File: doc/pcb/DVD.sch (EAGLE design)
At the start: 48 parts, among them IC1 7805, IC2 74HC14N

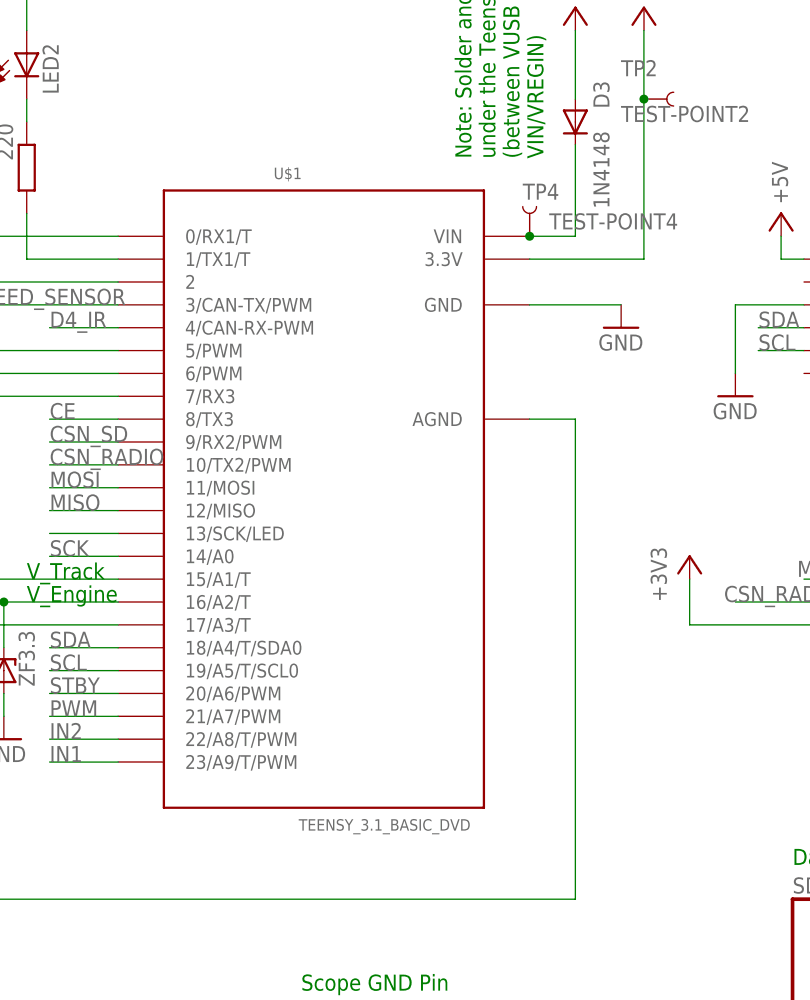
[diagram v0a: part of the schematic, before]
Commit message: bigger pads for Teensy
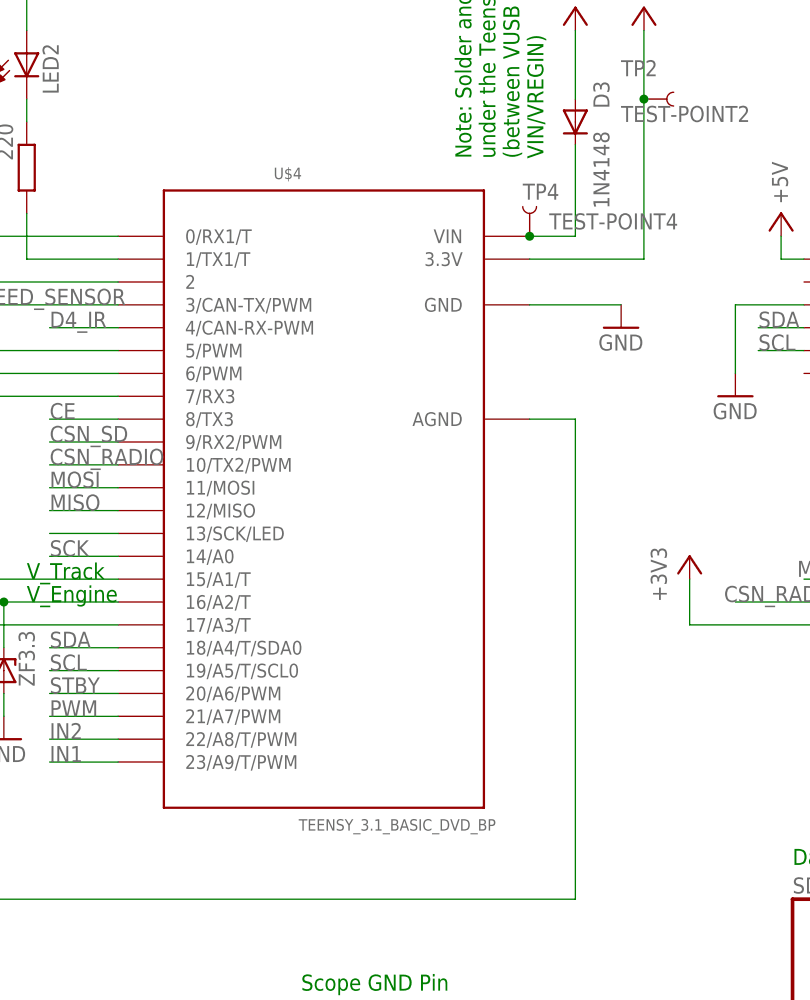
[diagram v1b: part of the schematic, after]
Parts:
- removed U$1: TEENSY_3.1_BASIC_DVD, Teensy_3_Series_Board_v1.0:TEENSY_3.1_BASIC_DVD
- added U$4: TEENSY_3.1_BASIC_DVD_BP, Teensy_3_Series_Board_v1.0:TEENSY_3.1_BASIC_DVD_BP
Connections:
- net +3V3: now also U$4.3.3V; no longer U$1.3.3V
- net AGND: now also U$4.AGND; no longer U$1.AGND
- net CE: now also U$4.8/TX3; no longer U$1.8/TX3
- net CSN_RADIO: now also U$4.10/TX2/PWM; no longer U$1.10/TX2/PWM
- net CSN_SD: now also U$4.9/RX2/PWM; no longer U$1.9/RX2/PWM
- net D4_IR: now also U$4.4/CAN-RX-PWM; no longer U$1.4/CAN-RX-PWM
- net GND: now also U$4.GND; no longer U$1.GND
- net IN1: now also U$4.23/A9/T/PWM; no longer U$1.23/A9/T/PWM
- net IN2: now also U$4.22/A8/T/PWM; no longer U$1.22/A8/T/PWM
- net MISO: now also U$4.12/MISO; no longer U$1.12/MISO
- net MOSI: now also U$4.11/MOSI; no longer U$1.11/MOSI
- net N$1: now also U$4.VIN; no longer U$1.VIN
- net N$10: now also U$4.15/A1/T; no longer U$1.15/A1/T
- net N$11: now also U$4.16/A2/T; no longer U$1.16/A2/T
- net N$18: now also U$4.0/RX1/T; no longer U$1.0/RX1/T
- net N$19: now also U$4.1/TX1/T; no longer U$1.1/TX1/T
- net N$20: now also U$4.2; no longer U$1.2
- net N$21: now also U$4.6/PWM; no longer U$1.6/PWM
- net N$22: now also U$4.7/RX3; no longer U$1.7/RX3
- net N$3: now also U$4.5/PWM; no longer U$1.5/PWM
- net N$6: now also U$4.17/A3/T; no longer U$1.17/A3/T
- net N$9: now also U$4.13/SCK/LED; no longer U$1.13/SCK/LED
- net PWM: now also U$4.21/A7/PWM; no longer U$1.21/A7/PWM
- net SCK: now also U$4.14/A0; no longer U$1.14/A0
- net SCL: now also U$4.19/A5/T/SCL0; no longer U$1.19/A5/T/SCL0
- net SDA: now also U$4.18/A4/T/SDA0; no longer U$1.18/A4/T/SDA0
- net SPEED_SENSOR: now also U$4.3/CAN-TX/PWM; no longer U$1.3/CAN-TX/PWM
- net STBY: now also U$4.20/A6/PWM; no longer U$1.20/A6/PWM

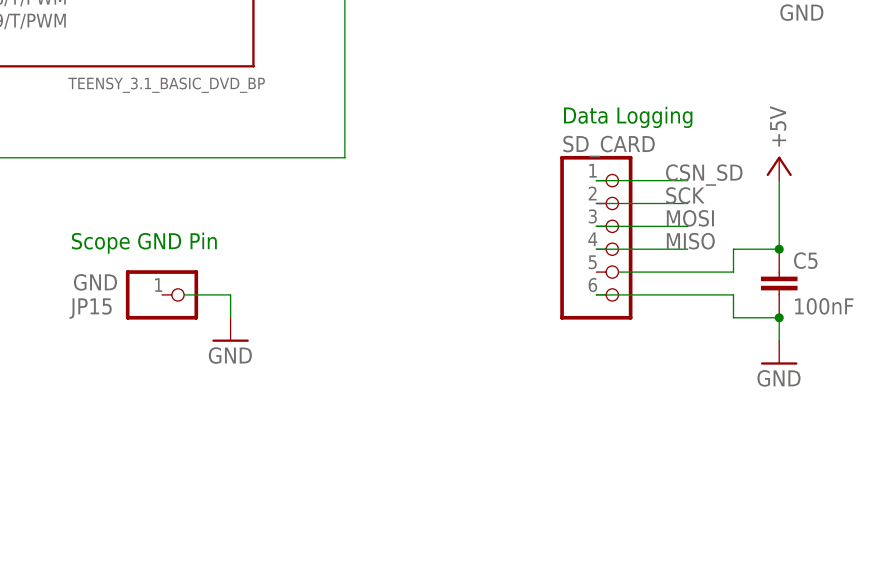
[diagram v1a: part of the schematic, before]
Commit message: Redrawn Chassis Picture, fixed schematic and created Board
Please review and give comments
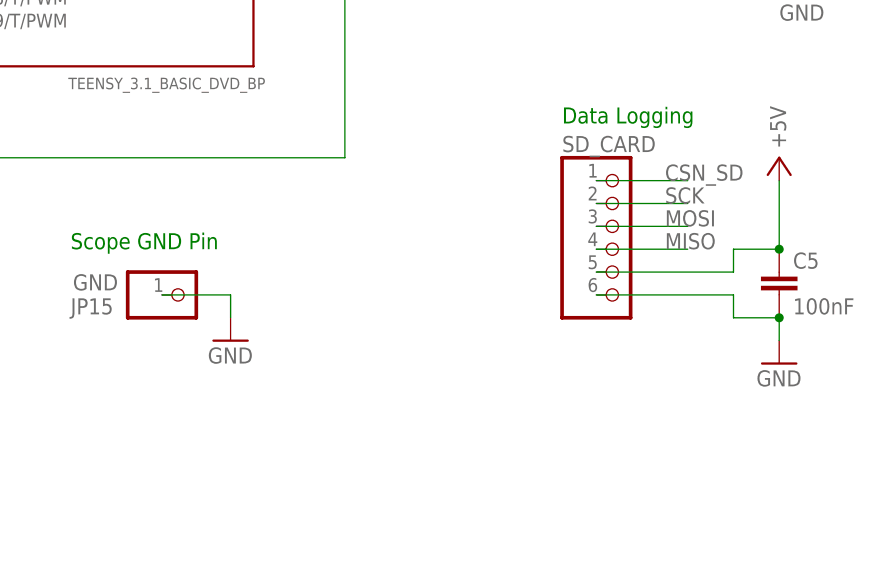
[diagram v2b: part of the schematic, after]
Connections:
- net +5V: now also SD_CARD.5
- net GND: now also JP15.1
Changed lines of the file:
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@@
 <segment>
 <pinref part="GND9" gate="1" pin="GND"/>
-<wire x1="139.7" y1="38.1" x2="144.78" y2="38.1" width="0.1524" layer="91"/>
+<wire x1="137.16" y1="38.1" x2="144.78" y2="38.1" width="0.1524" layer="91"/>
 <wire x1="144.78" y1="38.1" x2="144.78" y2="35.56" width="0.1524" layer="91"/>
+<pinref part="JP15" gate="G$1" pin="1"/>
 </segment>
 </net>
@@
 <pinref part="C5" gate="G$1" pin="1"/>
 <wire x1="205.74" y1="50.8" x2="205.74" y2="43.18" width="0.1524" layer="91"/>
-<wire x1="187.96" y1="40.64" x2="200.66" y2="40.64" width="0.1524" layer="91"/>
+<wire x1="185.42" y1="40.64" x2="200.66" y2="40.64" width="0.1524" layer="91"/>
 <wire x1="200.66" y1="40.64" x2="200.66" y2="43.18" width="0.1524" layer="91"/>
 <wire x1="200.66" y1="43.18" x2="205.74" y2="43.18" width="0.1524" layer="91"/>
 <junction x="205.74" y="43.18"/>
+<pinref part="SD_CARD" gate="A" pin="5"/>
 </segment>
 <segment>

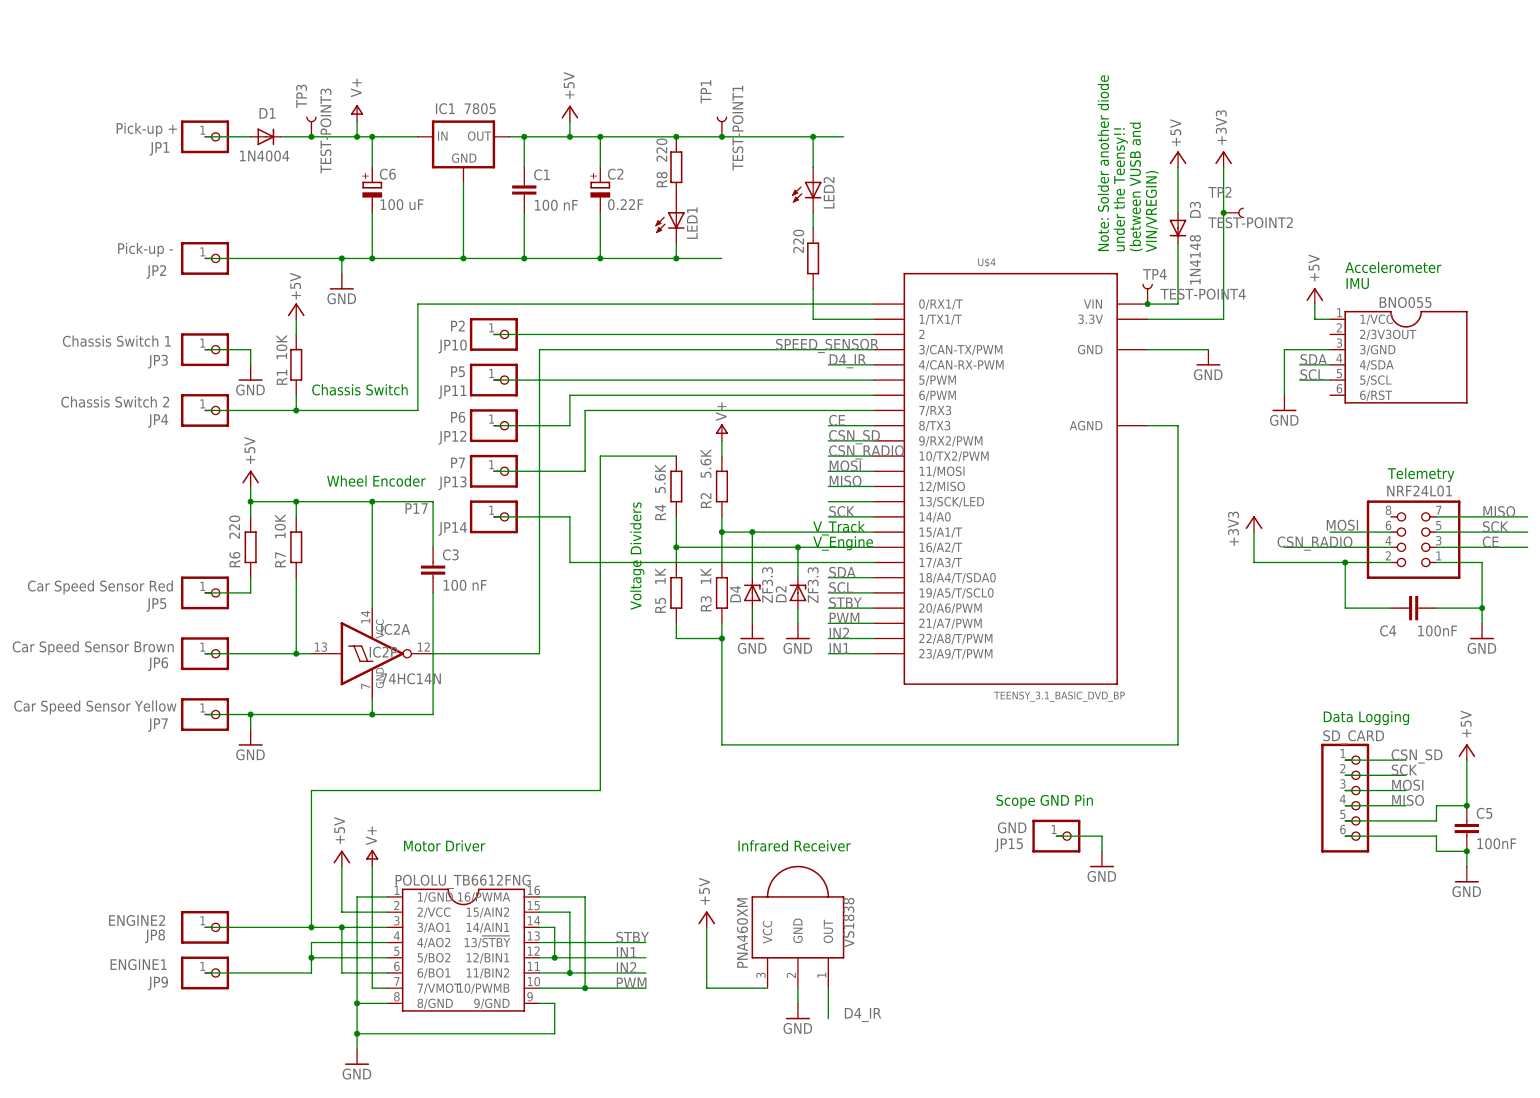
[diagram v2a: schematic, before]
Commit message: Schematics and PCB Updates
Schematics:
- connected all unused gates of 7414 to GND because open
  inputs may draw a lot of current
- renamed net for PickUp+ so that I can find it in the PCB
- went through ERC

PCB:
- made some tracks wider (power tracks)
- fixed DRC errors, default ones and also from the PCB
  manufacturer.
  *****NOTE****** 200+ DRC for the solder mask still
  *************** present.  I only fixed the ones for
  *************** the tracks and dimensions
- I had the copper pour up to the board outer dimension
  but that got reset when loading the DRC rules from
  dirty cheap PCBs (the manufacturer, see their "about"
  page)
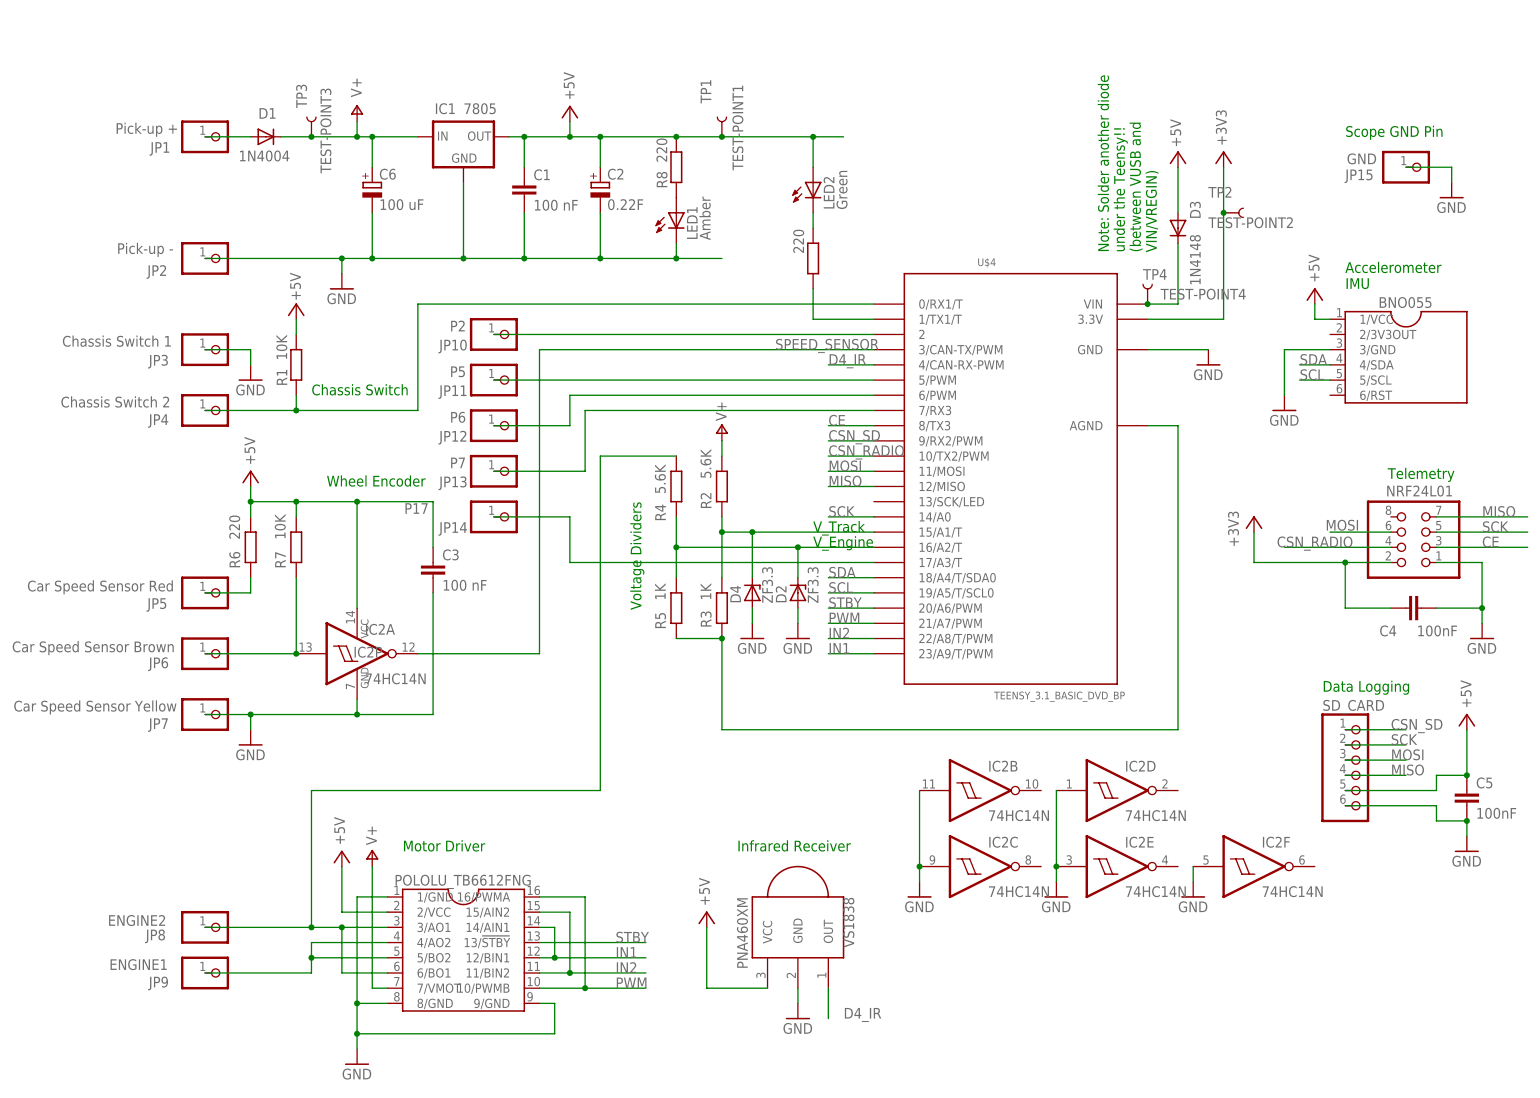
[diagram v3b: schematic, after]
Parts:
- LED1: value (none) -> Amber
- LED2: value (none) -> Green
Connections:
- net N$5 renamed PICKUP_PLUS
- removed net N$9: U$4.13/SCK/LED
- net GND: now also IC2B.I, IC2C.I, IC2D.I, IC2E.I, IC2F.I
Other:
- moved on the sheet: C5, IC2A, IC2P, JP15, R3, R5, SD_CARD

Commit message: PCB: new pads, ripup, partial route
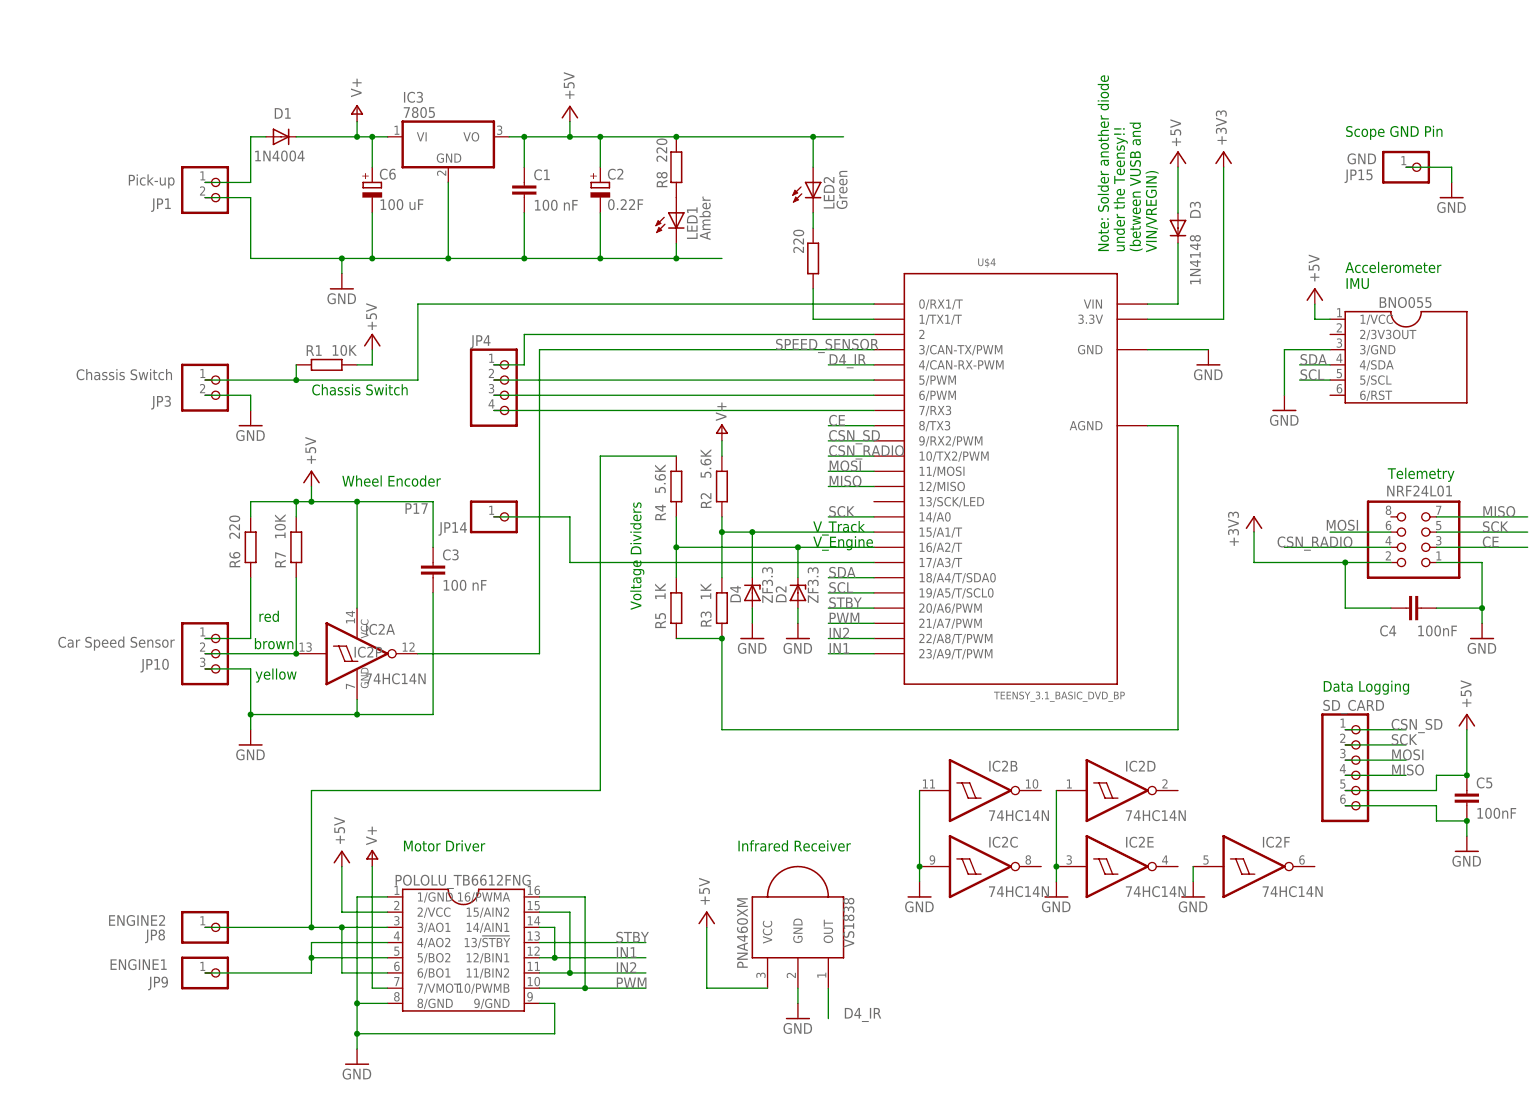
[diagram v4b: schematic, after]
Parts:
- removed IC1: 7805, v-reg:78XXL
- removed JP11: P5, pinhead:PINHD-1X1
- removed JP12: P6, pinhead:PINHD-1X1
- removed JP13: P7, pinhead:PINHD-1X1
- removed JP2: Pick-up -, pinhead:PINHD-1X1
- removed JP5: Car Speed Sensor Red, pinhead:PINHD-1X1
- removed JP6: Car Speed Sensor Brown, pinhead:PINHD-1X1
- removed JP7: Car Speed Sensor Yellow, pinhead:PINHD-1X1
- removed TP1: TEST-POINT1, SparkFun-Passives:TEST-POINT3
- removed TP2: TEST-POINT2, SparkFun-Passives:TEST-POINT3
- removed TP3: TEST-POINT3, SparkFun-Passives:TEST-POINT3
- removed TP4: TEST-POINT4, SparkFun-Passives:TEST-POINT3
- added IC3: 7805, linear:786TV
- D2, D4: device diode:ZENER-DIODEZD-2.5 -> diode:ZENER-DIODEZD-7.5
- JP1: value Pick-up + -> Pick-up; device pinhead:PINHD-1X1 -> pinhead:PINHD-1X2
- JP10: value P2 -> Car Speed Sensor; device pinhead:PINHD-1X1 -> pinhead:PINHD-1X3
- JP3: value Chassis Switch 1 -> Chassis Switch; device pinhead:PINHD-1X1 -> pinhead:PINHD-1X2
- JP4: value Chassis Switch 2 -> (none); device pinhead:PINHD-1X1 -> pinhead:PINHD-1X4
- R1, R2, R3, R4, R5, R6, R7, R8, R9: device resistor:R-EU_0204/7 -> resistor:R-EU_0207/10
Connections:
- net +3V3: no longer TP2.1
- net +5V: now also IC3.VO; no longer IC1.OUT, TP1.1
- net GND: now also JP1.2, JP10.3, JP3.2; no longer IC1.GND, JP2.1, JP3.1, JP7.1
- net N$1: no longer TP4.1
- net N$18: now also JP3.1; no longer JP4.1
- net N$2: now also JP10.1; no longer JP5.1
- net N$20: now also JP4.1; no longer JP10.1
- net N$21: now also JP4.3; no longer JP12.1
- net N$22: now also JP4.4; no longer JP13.1
- net N$26: now also JP10.2; no longer JP6.1
- net N$3: now also JP4.2; no longer JP11.1
- net V+: now also IC3.VI; no longer IC1.IN, TP3.1
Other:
- note added: "brown"
- note added: "red"
- note added: "yellow"
- moved on the sheet: D1, R1
